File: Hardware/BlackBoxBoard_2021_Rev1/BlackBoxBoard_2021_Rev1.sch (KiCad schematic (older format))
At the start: 18 parts

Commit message: Placed Pins to the TIVA and connected the Pins to both SD Cards
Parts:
- added J?: SD_Card2, symbol Connector:SD_Card
- added J?: SD_Card1, symbol Connector:SD_Card
- Conn? (x2): symbol MRDT_Connectors:AndersonPP -> BlackBoxBoard_2021_Rev1-rescue:AndersonPP-MRDT_Connectors
- J?: symbol MRDT_Connectors:Test_Point -> BlackBoxBoard_2021_Rev1-rescue:Test_Point-MRDT_Connectors
- U? (x8): symbol MRDT_Shields:TM4C129E_Launchpad -> BlackBoxBoard_2021_Rev1-rescue:TM4C129E_Launchpad-MRDT_Shields
- U?: symbol MRDT_Devices:LM2576D2TR4 -> BlackBoxBoard_2021_Rev1-rescue:LM2576D2TR4-MRDT_Devices
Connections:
- net +3V3: now also U?.+3V3 (A1_1), U?.+3V3' (A2_1), J?.4 (VDD), J?.4 (VDD)
- net GND: now also U?.GND (B1_2), U?.GND (B2_2), U?.GND (D1_1), U?.GND (D2_1), J?.3 (VSS), J?.3 (VSS), J?.6 (VSS), J?.6 (VSS)
- net SD1_SerialClock: now reaches U?.PD3 (A1_7)
- net SD1_SerialClock: now also J?.5 (CLK)
- net SD1_SerialData_Out: now reaches U?.PE4 (A1_2)
- net SD1_SerialData_Out: now also J?.2 (CMD)
- net SD1_SerialData_In: now reaches U?.PE5 (A1_6)
- net SD1_SerialData_In: now also J?.7 (DAT0)
- net Error_LED: now reaches U?.PF1 (C1_1)
- net Data_Write_LED: now reaches U?.PF2 (C1_2)
- net SD2_SerialClock: now reaches U?.PF3 (C1_3)
- net SD2_SerialClock: now also J?.5 (CLK)
- net Full_SD1_LED: now reaches U?.PG0 (C1_4)
- net Full_SD2_LED: now reaches U?.PL0 (C1_7)
- net SD1_ChipSelect: now reaches U?.PD2 (A2_2)
- net SD1_ChipSelect: now also J?.1 (CD/DAT3)
- net SD2_ChipSelect: now reaches U?.PQ1 (D2_9)
- net SD2_ChipSelect: now also J?.1 (CD/DAT3)
- net SD2_SerialData_OutRX: now reaches U?.PQ2 (D2_6)
- net SD2_SerialData_InTX: now reaches U?.PQ3 (D2_7)
- net SD2_SerialData_InTX: now also J?.7 (DAT0)
- new net Sd2_SerialData_OutRX: J?.2 (CMD)
- no-connect marks 0 -> 62
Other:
- moved on the sheet: U?C, U?D, U?G, U?H

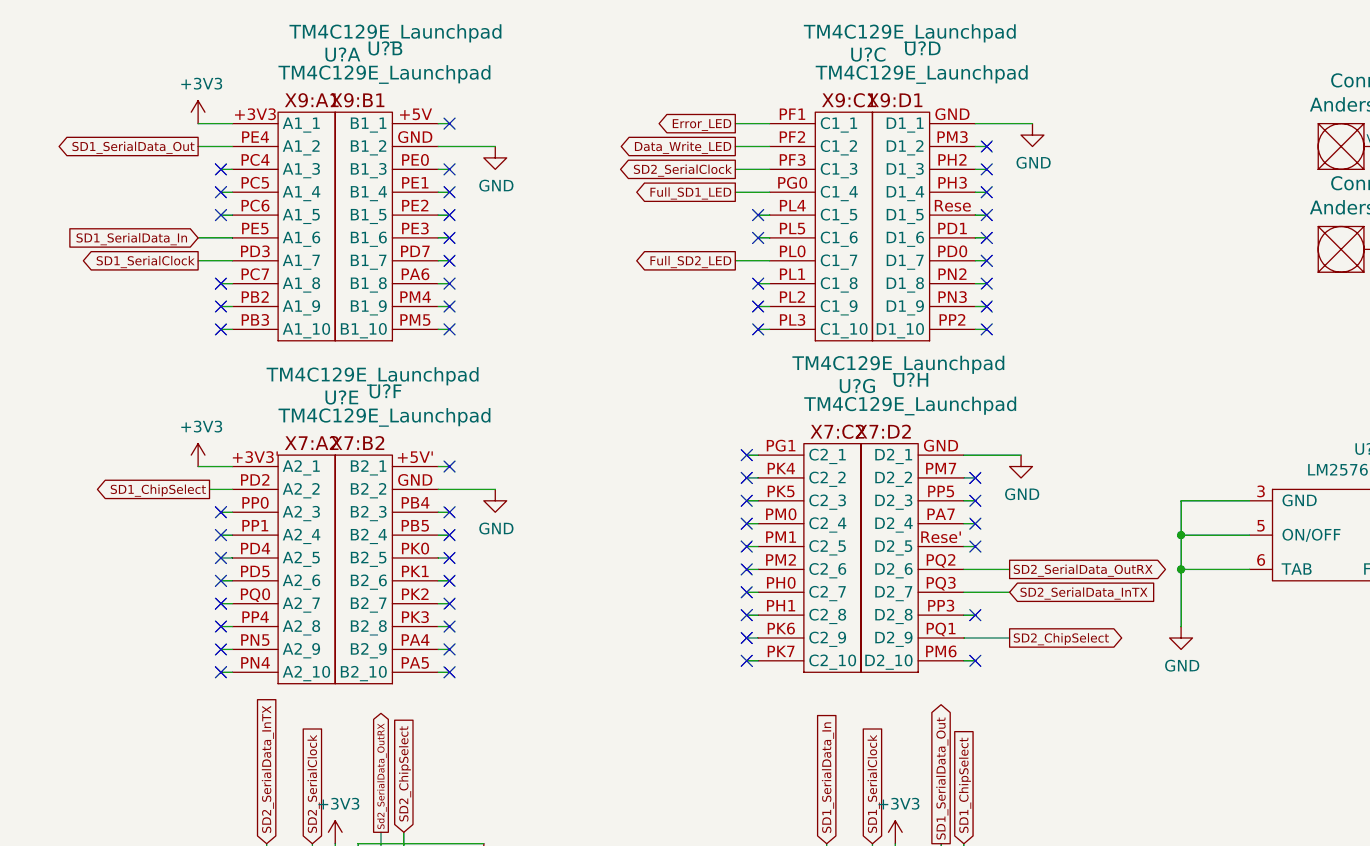
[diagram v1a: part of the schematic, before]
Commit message: Switched from Tiva to Pi
All that's left is finding the correct pins for the SDcard1
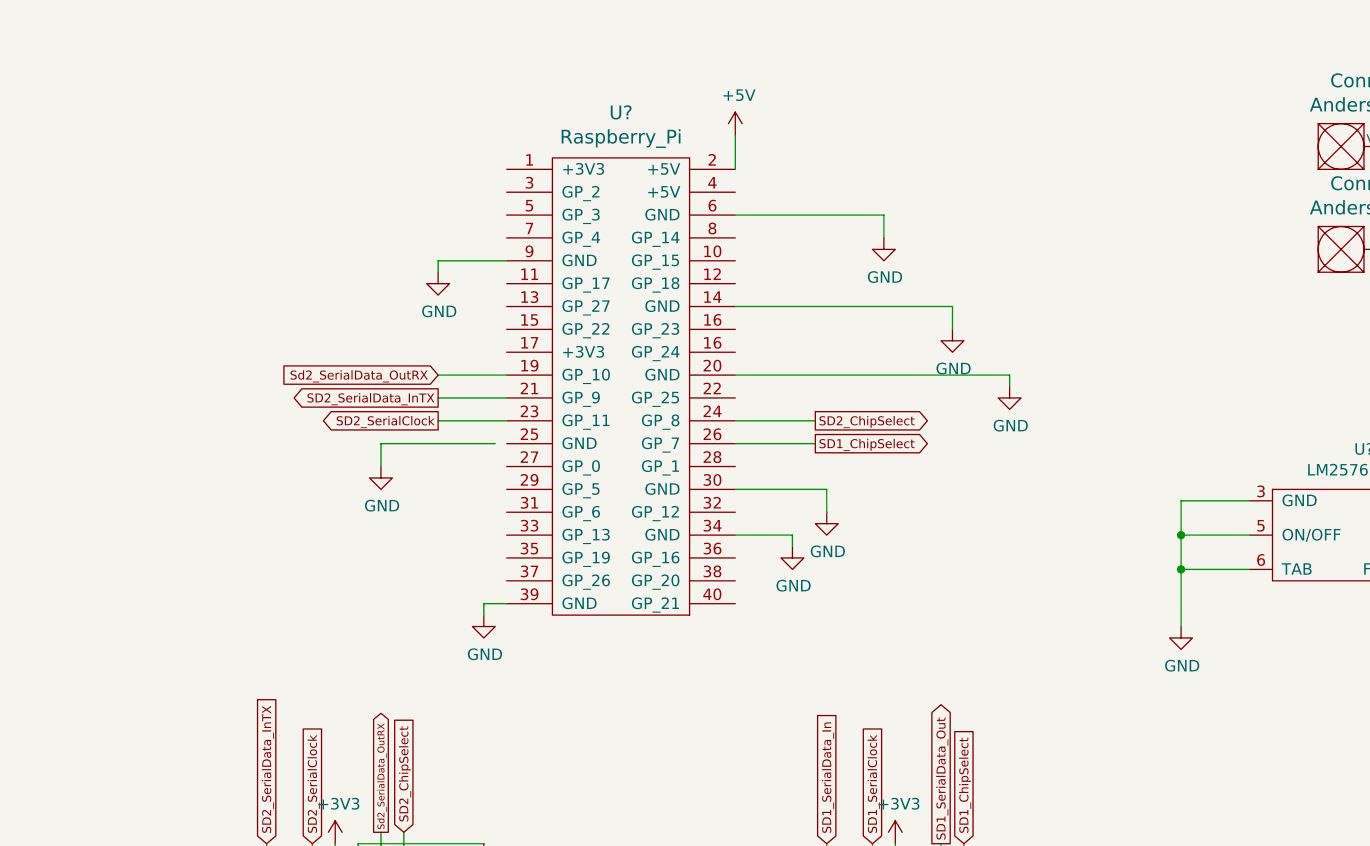
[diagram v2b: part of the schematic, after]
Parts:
- removed U? (x8): TM4C129E_Launchpad, symbol BlackBoxBoard_2021_Rev1-rescue:TM4C129E_Launchpad-MRDT_Shields
- added U?: Raspberry_Pi, symbol MRDT_Shields:Raspberry_Pi
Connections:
- net GND: now also U?.14 (GND), U?.20 (GND), U?.30 (GND), U?.34 (GND), U?.39 (GND), U?.6 (GND), U?.9 (GND)
- net SD1_ChipSelect: now also U?.26 (GP_7)
- net SD2_ChipSelect: now also U?.24 (GP_8)
- net SD2_SerialClock: now also U?.23 (GP_11)
- net SD2_SerialData_InTX: now also U?.21 (GP_9)
- net Sd2_SerialData_OutRX: now also U?.19 (GP_10)
- new net +5V: U?.2 (+5V)
- no-connect marks 62 -> 0
